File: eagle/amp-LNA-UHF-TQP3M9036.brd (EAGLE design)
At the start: 25 x 20 mm, 18 parts, among them J1 142-0701-851, J2 142-0701-851, U1 TQP3M903X

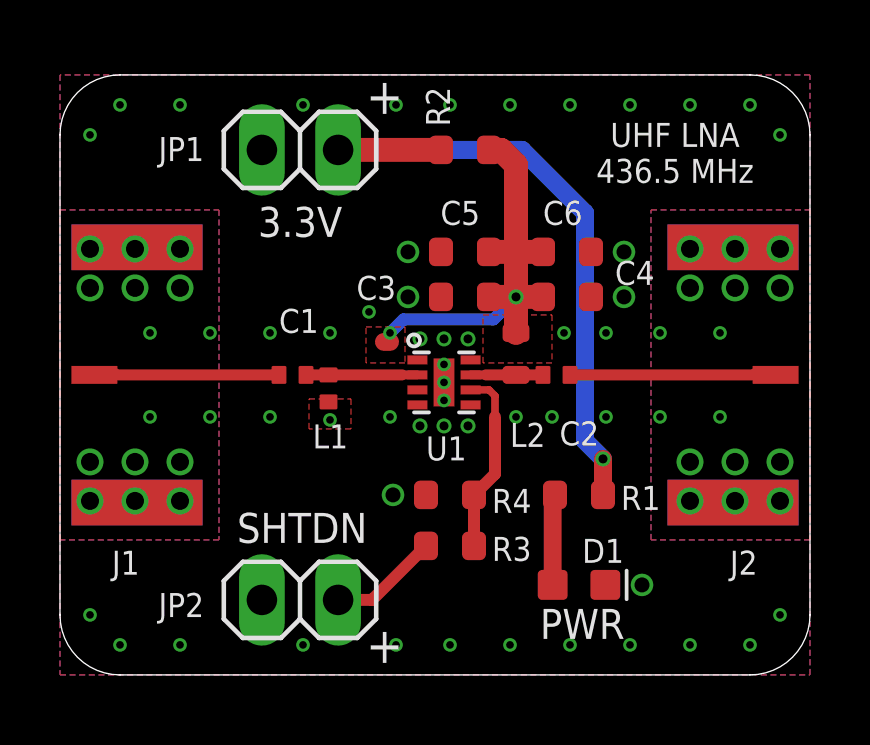
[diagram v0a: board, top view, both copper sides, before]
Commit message: Change SMA via sizes
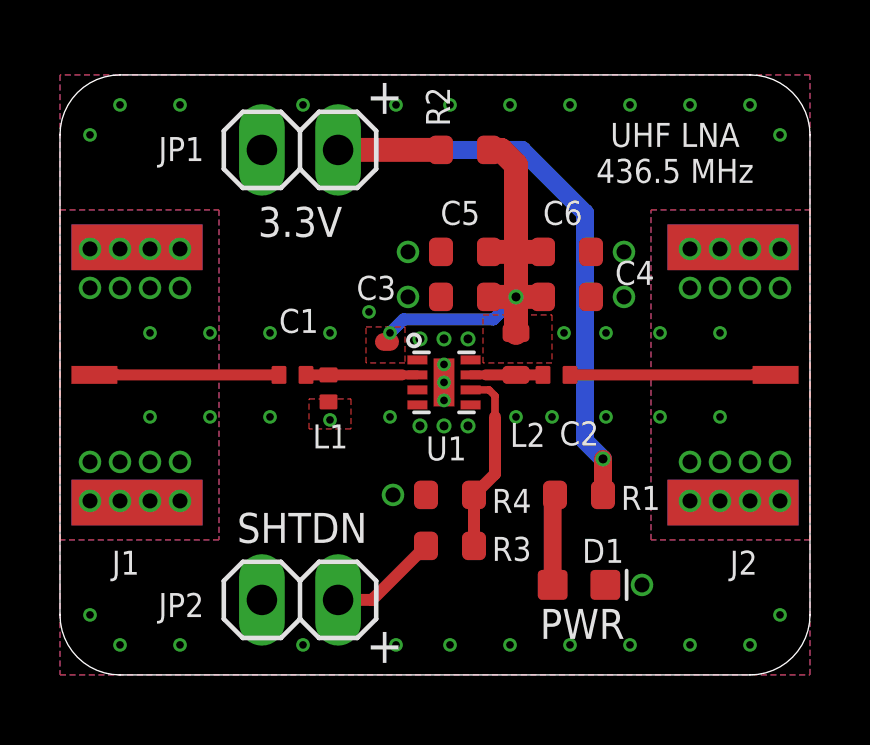
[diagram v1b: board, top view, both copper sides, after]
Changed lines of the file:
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@@
 <vertex x="0" y="20"/>
 </polygon>
-<via x="1" y="7.1" extent="1-16" drill="0.6"/>
-<via x="2.5" y="7.1" extent="1-16" drill="0.6"/>
-<via x="4" y="7.1" extent="1-16" drill="0.6"/>
-<via x="1" y="5.8" extent="1-16" drill="0.6"/>
-<via x="2.5" y="5.8" extent="1-16" drill="0.6"/>
-<via x="4" y="5.8" extent="1-16" drill="0.6"/>
-<via x="1" y="12.9" extent="1-16" drill="0.6"/>
-<via x="2.5" y="12.9" extent="1-16" drill="0.6"/>
-<via x="4" y="12.9" extent="1-16" drill="0.6"/>
-<via x="1" y="14.2" extent="1-16" drill="0.6"/>
-<via x="2.5" y="14.2" extent="1-16" drill="0.6"/>
-<via x="4" y="14.2" extent="1-16" drill="0.6"/>
-<via x="24" y="14.2" extent="1-16" drill="0.6"/>
-<via x="22.5" y="14.2" extent="1-16" drill="0.6"/>
-<via x="21" y="14.2" extent="1-16" drill="0.6"/>
-<via x="21" y="12.9" extent="1-16" drill="0.6"/>
-<via x="22.5" y="12.9" extent="1-16" drill="0.6"/>
-<via x="24" y="12.9" extent="1-16" drill="0.6"/>
-<via x="24" y="5.8" extent="1-16" drill="0.6"/>
-<via x="22.5" y="5.8" extent="1-16" drill="0.6"/>
-<via x="21" y="5.8" extent="1-16" drill="0.6"/>
-<via x="21" y="7.1" extent="1-16" drill="0.6"/>
-<via x="22.5" y="7.1" extent="1-16" drill="0.6"/>
-<via x="24" y="7.1" extent="1-16" drill="0.6"/>
+<via x="1" y="7.1" extent="1-16" drill="0.5"/>
+<via x="2" y="7.1" extent="1-16" drill="0.5"/>
+<via x="4" y="7.1" extent="1-16" drill="0.5"/>
+<via x="1" y="5.8" extent="1-16" drill="0.5"/>
+<via x="2" y="5.8" extent="1-16" drill="0.5"/>
+<via x="4" y="5.8" extent="1-16" drill="0.5"/>
+<via x="1" y="12.9" extent="1-16" drill="0.5"/>
+<via x="2" y="12.9" extent="1-16" drill="0.5"/>
+<via x="4" y="12.9" extent="1-16" drill="0.5"/>
+<via x="1" y="14.2" extent="1-16" drill="0.5"/>
+<via x="2" y="14.2" extent="1-16" drill="0.5"/>
+<via x="4" y="14.2" extent="1-16" drill="0.5"/>
+<via x="24" y="14.2" extent="1-16" drill="0.5"/>
+<via x="23" y="14.2" extent="1-16" drill="0.5"/>
+<via x="21" y="14.2" extent="1-16" drill="0.5"/>
+<via x="21" y="12.9" extent="1-16" drill="0.5"/>
+<via x="23" y="12.9" extent="1-16" drill="0.5"/>
+<via x="24" y="12.9" extent="1-16" drill="0.5"/>
+<via x="24" y="5.8" extent="1-16" drill="0.5"/>
+<via x="23" y="5.8" extent="1-16" drill="0.5"/>
+<via x="21" y="5.8" extent="1-16" drill="0.5"/>
+<via x="21" y="7.1" extent="1-16" drill="0.5"/>
+<via x="23" y="7.1" extent="1-16" drill="0.5"/>
+<via x="24" y="7.1" extent="1-16" drill="0.5"/>
 <via x="3" y="8.6" extent="1-16" drill="0.254"/>
 <via x="5" y="8.6" extent="1-16" drill="0.254"/>
@@
 <contactref element="C6" pad="2"/>
 <contactref element="L1" pad="2"/>
+<via x="3" y="12.9" extent="1-16" drill="0.5"/>
+<via x="3" y="14.2" extent="1-16" drill="0.5"/>
+<via x="3" y="5.8" extent="1-16" drill="0.5"/>
+<via x="3" y="7.1" extent="1-16" drill="0.5"/>
+<via x="22" y="7.1" extent="1-16" drill="0.5"/>
+<via x="22" y="5.8" extent="1-16" drill="0.5"/>
+<via x="22" y="12.9" extent="1-16" drill="0.5"/>
+<via x="22" y="14.2" extent="1-16" drill="0.5"/>
 </signal>
 <signal name="N$28" class="1">

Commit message: Update SMA footprint
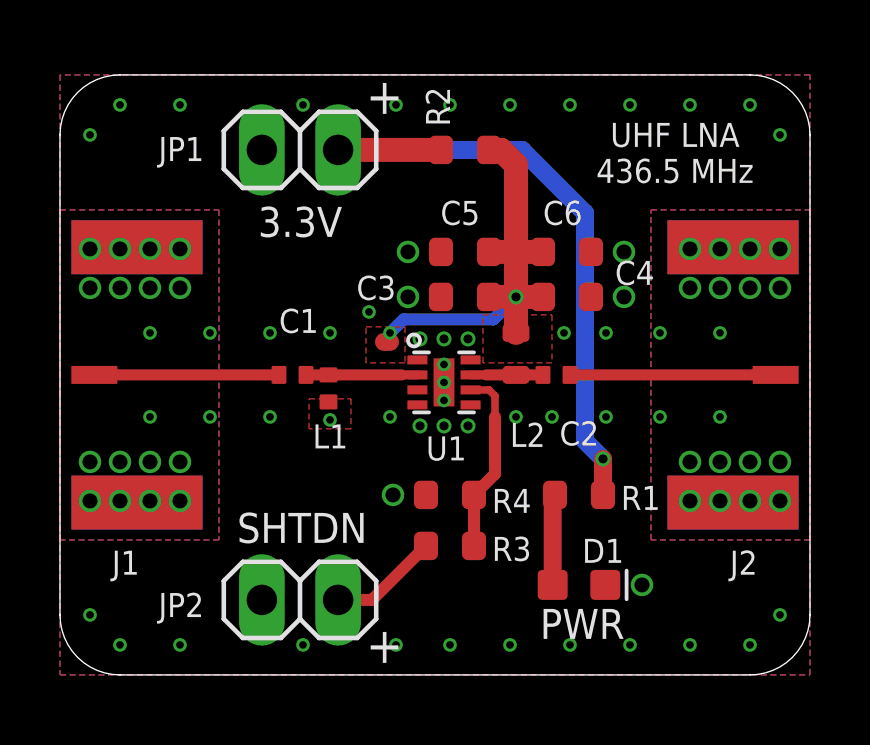
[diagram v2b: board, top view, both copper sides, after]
